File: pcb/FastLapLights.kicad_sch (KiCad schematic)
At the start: 17 parts, among them J1 POWER_CON, J2 SWD, J3 PWR, J4 I2C, J5 Conn_02x04_Counter_Clockwise, U1 BD33FC0FP, U2 STM32C011F4Px

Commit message: prep firmware
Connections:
- net IO_POWER_RAIL_DATA: now also U2.13 (PA6); no longer U2.12 (PA5)
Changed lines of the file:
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@@
-	)
-	(no_connect
-		(at 248.92 68.58)
 	)
 	(no_connect
@@
 	)
 	(no_connect
+		(at 248.92 66.04)
+	)
+	(no_connect
 		(at 248.92 76.2)
 	)
@@
 	(wire
 		(pts
-			(xy 248.92 66.04) (xy 267.97 66.04)
-		)
-		(stroke
-			(width 0)
-			(type default)
-		)
-	)
-	(wire
-		(pts
 			(xy 248.92 81.28) (xy 267.97 81.28)
 		)
@@
 		(pts
 			(xy 72.39 74.93) (xy 72.39 76.2)
+		)
+		(stroke
+			(width 0)
+			(type default)
+		)
+	)
+	(wire
+		(pts
+			(xy 248.92 68.58) (xy 267.97 68.58)
 		)
 		(stroke
@@
 		)
 	)
+	(label "IO_POWER_RAIL_DATA"
+		(at 267.97 68.58 180)
+		(effects
+			(font
+				(size 1.1 1.1)
+			)
+			(justify right bottom)
+		)
+	)
 	(label "VRAIL_CAP"
 		(at 49.53 68.58 0)
@@
 		(effects
 			(font
-				(size 1.1 1.1)
-			)
-			(justify right bottom)
-		)
-	)
-	(label "IO_POWER_RAIL_DATA"
-		(at 267.97 66.04 180)
-		(effects
-			(font

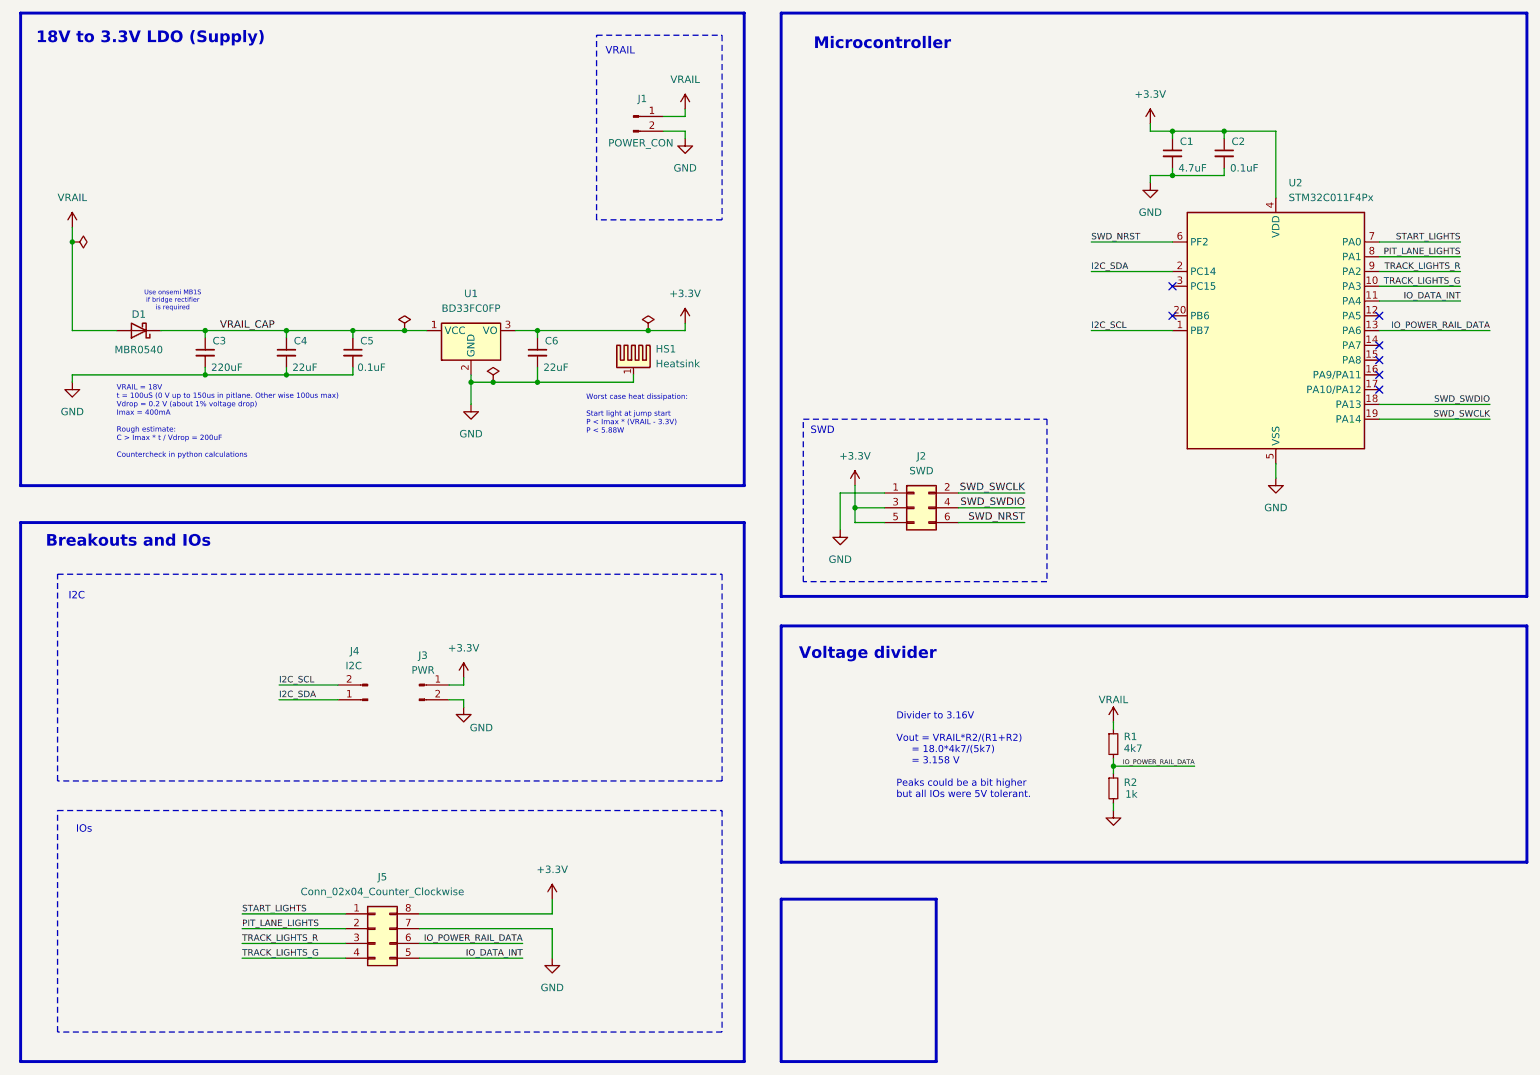
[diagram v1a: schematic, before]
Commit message: migrate track lights
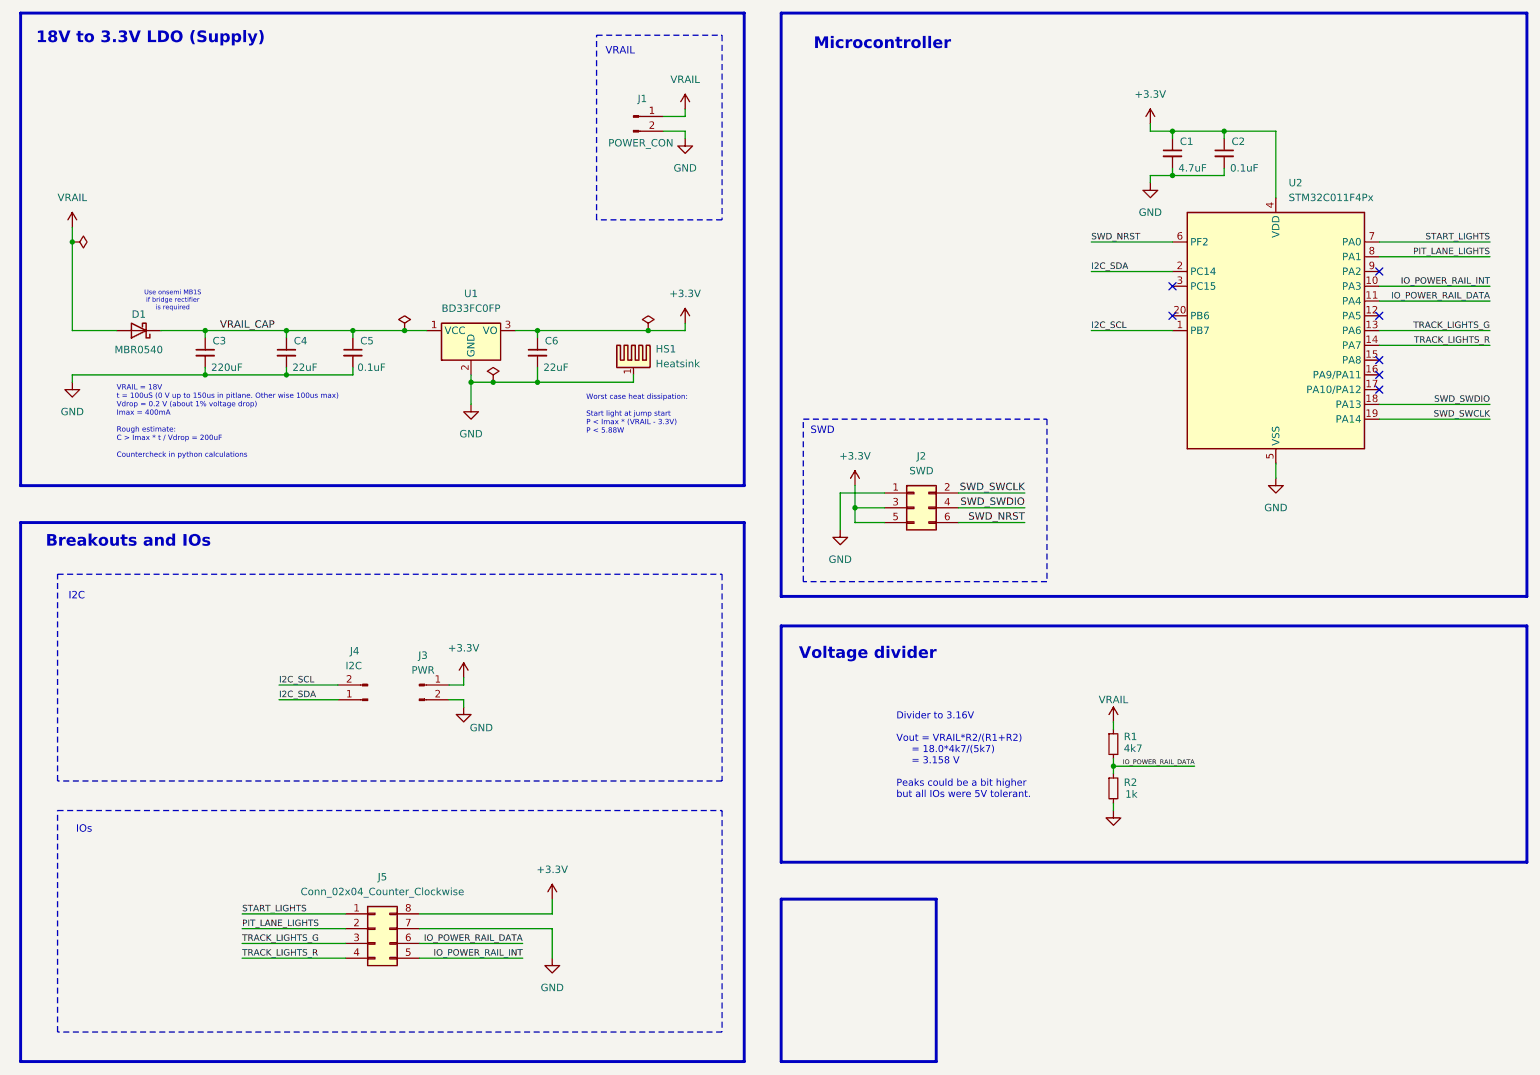
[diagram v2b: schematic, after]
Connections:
- net IO_POWER_RAIL_DATA: now also U2.11 (PA4); no longer U2.13 (PA6)
- net TRACK_LIGHTS_G: now also J5.3 (Pin_3), U2.13 (PA6); no longer J5.4 (Pin_4), U2.10 (PA3)
- net TRACK_LIGHTS_R: now also J5.4 (Pin_4), U2.14 (PA7); no longer J5.3 (Pin_3), U2.9 (PA2)
- net IO_DATA_INT renamed IO_POWER_RAIL_INT
- net IO_POWER_RAIL_INT: now also U2.10 (PA3); no longer U2.11 (PA4)
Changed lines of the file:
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@@
-	)
-	(no_connect
-		(at 248.92 71.12)
 	)
 	(no_connect
@@
 		(at 248.92 76.2)
 	)
-	(wire
-		(pts
-			(xy 248.92 53.34) (xy 262.89 53.34)
+	(no_connect
+		(at 248.92 58.42)
+	)
+	(wire
+		(pts
+			(xy 248.92 53.34) (xy 267.97 53.34)
 		)
 		(stroke
@@
 	(wire
 		(pts
-			(xy 248.92 60.96) (xy 262.89 60.96)
+			(xy 248.92 60.96) (xy 267.97 60.96)
 		)
 		(stroke
@@
 	(wire
 		(pts
-			(xy 248.92 55.88) (xy 262.89 55.88)
+			(xy 248.92 55.88) (xy 267.97 55.88)
 		)
 		(stroke
@@
 	(wire
 		(pts
+			(xy 248.92 71.12) (xy 267.97 71.12)
+		)
+		(stroke
+			(width 0)
+			(type default)
+		)
+	)
+	(wire
+		(pts
 			(xy 176.53 99.06) (xy 187.96 99.06)
 		)
@@
 	(wire
 		(pts
-			(xy 248.92 63.5) (xy 262.89 63.5)
+			(xy 248.92 63.5) (xy 267.97 63.5)
 		)
 		(stroke
@@
 		(pts
 			(xy 53.34 168.91) (xy 71.12 168.91)
-		)
-		(stroke
-			(width 0)
-			(type default)
-		)
-	)
-	(wire
-		(pts
-			(xy 248.92 58.42) (xy 262.89 58.42)
 		)
 		(stroke
@@
 	)
 	(label "PIT_LANE_LIGHTS"
-		(at 262.89 55.88 180)
-		(effects
-			(font
-				(size 1.1 1.1)
-			)
-			(justify right bottom)
-		)
-	)
-	(label "TRACK_LIGHTS_G"
-		(at 262.89 60.96 180)
+		(at 267.97 55.88 180)
+		(effects
+			(font
+				(size 1.1 1.1)
+			)
+			(justify right bottom)
+		)
+	)
+	(label "SWD_SWDIO"
+		(at 267.97 81.28 180)
 		(effects
 			(font
@@
 		)
 	)
+	(label "TRACK_LIGHTS_R"
+		(at 267.97 71.12 180)
+		(effects
+			(font
+				(size 1.1 1.1)
+			)
+			(justify right bottom)
+		)
+	)
+	(label "IO_POWER_RAIL_INT"
+		(at 267.97 60.96 180)
+		(effects
+			(font
+				(size 1.1 1.1)
+			)
+			(justify right bottom)
+		)
+	)
 	(label "I2C_SDA"
 		(at 59.69 132.08 0)
@@
 		)
 	)
-	(label "IO_POWER_RAIL_DATA"
-		(at 267.97 68.58 180)
-		(effects
-			(font
-				(size 1.1 1.1)
-			)
-			(justify right bottom)
-		)
-	)
 	(label "VRAIL_CAP"
 		(at 49.53 68.58 0)
@@
 		)
 	)
-	(label "SWD_SWDIO"
-		(at 267.97 81.28 180)
-		(effects
-			(font
-				(size 1.1 1.1)
-			)
-			(justify right bottom)
-		)
-	)
-	(label "TRACK_LIGHTS_R"
-		(at 53.34 173.99 0)
-		(effects
-			(font
-				(size 1.1 1.1)
-			)
-			(justify left bottom)
+	(label "TRACK_LIGHTS_G"
+		(at 267.97 68.58 180)
+		(effects
+			(font
+				(size 1.1 1.1)
+			)
+			(justify right bottom)
 		)
 	)
@@
 		)
 	)
+	(label "TRACK_LIGHTS_R"
+		(at 53.34 176.53 0)
+		(effects
+			(font
+				(size 1.1 1.1)
+			)
+			(justify left bottom)
+		)
+	)
 	(label "START_LIGHTS"
 		(at 53.34 168.91 0)
@@
 		)
 	)
-	(label "TRACK_LIGHTS_R"
-		(at 262.89 58.42 180)
-		(effects
-			(font
-				(size 1.1 1.1)
-			)
-			(justify right bottom)
-		)
-	)
 	(label "SWD_SWCLK"
 		(at 267.97 83.82 180)
@@
 	)
 	(label "START_LIGHTS"
-		(at 262.89 53.34 180)
-		(effects
-			(font
-				(size 1.1 1.1)
-			)
-			(justify right bottom)
-		)
-	)
-	(label "IO_DATA_INT"
+		(at 267.97 53.34 180)
+		(effects
+			(font
+				(size 1.1 1.1)
+			)
+			(justify right bottom)
+		)
+	)
+	(label "IO_POWER_RAIL_INT"
 		(at 101.6 176.53 180)
 		(effects
@@
 		)
 	)
+	(label "IO_POWER_RAIL_DATA"
+		(at 267.97 63.5 180)
+		(effects
+			(font
+				(size 1.1 1.1)
+			)
+			(justify right bottom)
+		)
+	)
 	(label "SWD_SWCLK"
 		(at 187.96 96.52 180)
@@
 		)
 	)
-	(label "IO_DATA_INT"
-		(at 262.89 63.5 180)
-		(effects
-			(font
-				(size 1.1 1.1)
-			)
-			(justify right bottom)
-		)
-	)
 	(label "TRACK_LIGHTS_G"
-		(at 53.34 176.53 0)
-		(effects
-			(font
+		(at 53.34 173.99 0)
+		(effects
+			(font
